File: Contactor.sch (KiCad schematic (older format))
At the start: 20 parts, among them J9 ContactorConn, Q1 NTR4003NT1G, Q2 VND5N07-E, U8 SI8261ABC-IS, U9 BAS70-04

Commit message: Moves BAS70-04 to utsvt-chips because other systems use this component
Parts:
- U9: symbol utsvt-bps:BAS70-04 -> utsvt-chips:BAS70-04
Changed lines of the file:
@@
 $EndComp
 $Comp
-L utsvt-bps:BAS70-04 U9
+L utsvt-chips:BAS70-04 U9
 U 1 1 5F133A4C
 P 8200 3500

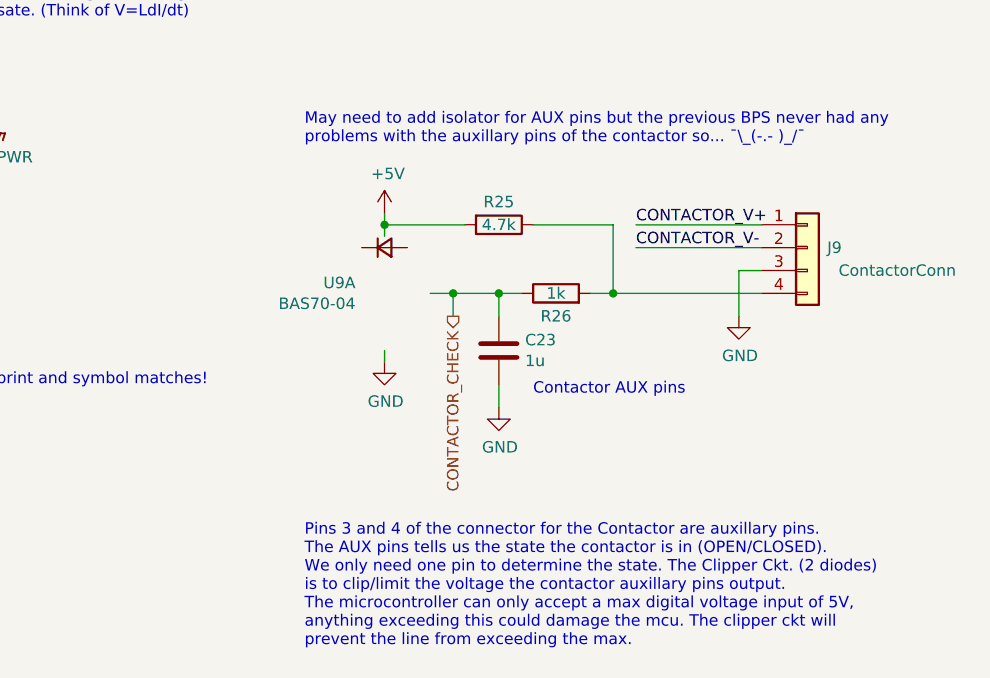
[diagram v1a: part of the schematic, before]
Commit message: Updates BAS70-04 footprint for Contactor auxillary interface
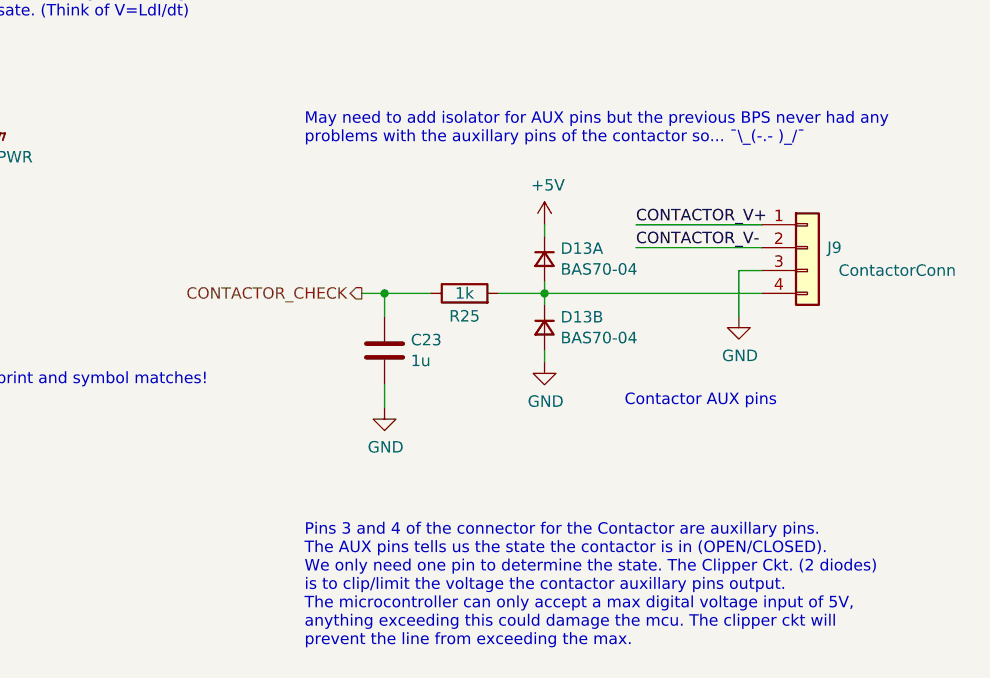
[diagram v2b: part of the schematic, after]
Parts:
- removed R25: 4.7k, Resistor_SMD:R_0805_2012Metric, symbol Device:R
- removed U9: BAS70-04, Package_TO_SOT_SMD:SOT-23, symbol utsvt-chips:BAS70-04
- added D13: BAS70-04, Package_TO_SOT_SMD:SOT-23, symbol utsvt-chips:BAS70-04
- renumbered R26 to R25
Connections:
- wire segments 78 -> 74
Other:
- moved on the sheet: C23, R25
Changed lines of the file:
@@
 $EndComp
 $Comp
-L power:GND #PWR061
+L power:GND #PWR063
 U 1 1 5C30292A
 P 9750 3800
-F 0 "#PWR061" H 9750 3550 50  0001 C CNN
+F 0 "#PWR063" H 9750 3550 50  0001 C CNN
 F 1 "GND" H 9755 3627 50  0000 C CNN
 F 2 "" H 9750 3800 50  0001 C CNN
@@
 $EndComp
 $Comp
-L Device:R R26
+L Device:R R25
 U 1 1 5C302C24
-P 8950 3700
-F 0 "R26" V 8850 3700 50  0000 C CNN
-F 1 "1k" V 8950 3700 50  0000 C CNN
-F 2 "Resistor_SMD:R_0805_2012Metric" V 8880 3700 50  0001 C CNN
-F 3 "~" H 8950 3700 50  0001 C CNN
-	1    8950 3700
+P 8550 3700
+F 0 "R25" V 8450 3700 50  0000 C CNN
+F 1 "1k" V 8550 3700 50  0000 C CNN
+F 2 "Resistor_SMD:R_0805_2012Metric" V 8480 3700 50  0001 C CNN
+F 3 "~" H 8550 3700 50  0001 C CNN
+	1    8550 3700
 	0    -1   -1   0
 $EndComp
 Wire Wire Line
 	9750 3800 9750 3600
-Wire Wire Line
-	9850 3700 9200 3700
 $Comp
 L Device:C C23
 U 1 1 5C3030F2
-P 8700 3950
-F 0 "C23" H 8815 3996 50  0000 L CNN
-F 1 "1u" H 8815 3905 50  0000 L CNN
-F 2 "Capacitor_SMD:C_0805_2012Metric" H 8738 3800 50  0001 C CNN
-F 3 "~" H 8700 3950 50  0001 C CNN
-	1    8700 3950
-	1    0    0    -1
-$EndComp
-Wire Wire Line
-	8700 3800 8700 3700
-Wire Wire Line
-	8700 3700 8800 3700
-Wire Wire Line
-	8700 4200 8700 4100
+P 8200 3950
+F 0 "C23" H 8315 3996 50  0000 L CNN
+F 1 "1u" H 8315 3905 50  0000 L CNN
+F 2 "Capacitor_SMD:C_0805_2012Metric" H 8238 3800 50  0001 C CNN
+F 3 "~" H 8200 3950 50  0001 C CNN
+	1    8200 3950
+	1    0    0    -1
+$EndComp
+Wire Wire Line
+	8200 3800 8200 3700
+Wire Wire Line
+	8200 3700 8400 3700
+Wire Wire Line
+	8200 4200 8200 4100
 $Comp
 L power:GND #PWR060
 U 1 1 5C304D16
-P 8700 4200
-F 0 "#PWR060" H 8700 3950 50  0001 C CNN
-F 1 "GND" H 8705 4027 50  0000 C CNN
-F 2 "" H 8700 4200 50  0001 C CNN
-F 3 "" H 8700 4200 50  0001 C CNN
-	1    8700 4200
-	1    0    0    -1
-$EndComp
-Connection ~ 8700 3700
-$Comp
-L power:GND #PWR059
+P 8200 4200
+F 0 "#PWR060" H 8200 3950 50  0001 C CNN
+F 1 "GND" H 8205 4027 50  0000 C CNN
+F 2 "" H 8200 4200 50  0001 C CNN
+F 3 "" H 8200 4200 50  0001 C CNN
+	1    8200 4200
+	1    0    0    -1
+$EndComp
+Connection ~ 8200 3700
+$Comp
+L power:GND #PWR062
 U 1 1 5C305432
-P 8200 4000
-F 0 "#PWR059" H 8200 3750 50  0001 C CNN
-F 1 "GND" H 8205 3827 50  0000 C CNN
-F 2 "" H 8200 4000 50  0001 C CNN
-F 3 "" H 8200 4000 50  0001 C CNN
-	1    8200 4000
-	1    0    0    -1
-$EndComp
-Wire Wire Line
-	8200 4000 8200 3950
-$Comp
-L power:+5V #PWR058
+P 8900 4000
+F 0 "#PWR062" H 8900 3750 50  0001 C CNN
+F 1 "GND" H 8905 3827 50  0000 C CNN
+F 2 "" H 8900 4000 50  0001 C CNN
+F 3 "" H 8900 4000 50  0001 C CNN
+	1    8900 4000
+	1    0    0    -1
+$EndComp
+Wire Wire Line
+	8900 4000 8900 3950
+$Comp
+L power:+5V #PWR061
 U 1 1 5C305723
-P 8200 3350
-F 0 "#PWR058" H 8200 3200 50  0001 C CNN
-F 1 "+5V" H 8215 3523 50  0000 C CNN
-F 2 "" H 8200 3350 50  0001 C CNN
-F 3 "" H 8200 3350 50  0001 C CNN
-	1    8200 3350
-	1    0    0    -1
-$EndComp
-Text HLabel 8500 3800 3    50   Output ~ 0
+P 8900 3400
+F 0 "#PWR061" H 8900 3250 50  0001 C CNN
+F 1 "+5V" H 8915 3573 50  0000 C CNN
+F 2 "" H 8900 3400 50  0001 C CNN
+F 3 "" H 8900 3400 50  0001 C CNN
+	1    8900 3400
+	1    0    0    -1
+$EndComp
+Text HLabel 8100 3700 0    50   Output ~ 0
 CONTACTOR_CHECK
-Wire Wire Line
-	8500 3800 8500 3700
-Connection ~ 8500 3700
-Wire Wire Line
-	8500 3700 8700 3700
-Wire Wire Line
-	8400 3700 8500 3700
 Wire Wire Line
 	9850 3500 9300 3500
@@
 Wire Wire Line
 	2350 3550 2350 3500
-$Comp
-L Device:R R25
-U 1 1 5C3945DD
-P 8700 3400
-F 0 "R25" V 8600 3400 50  0000 C CNN
-F 1 "4.7k" V 8700 3400 50  0000 C CNN
-F 2 "Resistor_SMD:R_0805_2012Metric" V 8630 3400 50  0001 C CNN
-F 3 "~" H 8700 3400 50  0001 C CNN
-	1    8700 3400
-	0    1    1    0
-$EndComp
-Wire Wire Line
-	8200 3350 8200 3400
-Wire Wire Line
-	8200 3400 8550 3400
-Connection ~ 8200 3400
-Wire Wire Line
-	8200 3400 8200 3450
-Wire Wire Line
-	8850 3400 9200 3400
-Wire Wire Line
-	9200 3400 9200 3700
-Connection ~ 9200 3700
-Wire Wire Line
-	9200 3700 9100 3700
-$Comp
-L power:GNDPWR #PWR056
+Wire Wire Line
+	8900 3400 8900 3450
+$Comp
+L power:GNDPWR #PWR058
 U 1 1 5C3F7F9B
 P 5800 4450
-F 0 "#PWR056" H 5800 4250 50  0001 C CNN
+F 0 "#PWR058" H 5800 4250 50  0001 C CNN
 F 1 "GNDPWR" H 5804 4296 50  0000 C CNN
 F 2 "" H 5800 4400 50  0001 C CNN
@@
 $EndComp
 $Comp
-L power:GNDPWR #PWR052
+L power:GNDPWR #PWR054
 U 1 1 5C3FD54A
 P 4400 4050
-F 0 "#PWR052" H 4400 3850 50  0001 C CNN
+F 0 "#PWR054" H 4400 3850 50  0001 C CNN
 F 1 "GNDPWR" H 4404 3896 50  0000 C CNN
 F 2 "" H 4400 4000 50  0001 C CNN
@@
 P 2350 4700
 AR Path="/5C392C6A/5C9B866F" Ref="#PWR?"  Part="1"
-AR Path="/5C38C674/5C9B866F" Ref="#PWR050"  Part="1"
-F 0 "#PWR050" H 2350 4450 50  0001 C CNN
+AR Path="/5C38C674/5C9B866F" Ref="#PWR052"  Part="1"
+F 0 "#PWR052" H 2350 4450 50  0001 C CNN
 F 1 "GND" H 2355 4527 50  0000 C CNN
 F 2 "" H 2350 4700 50  0001 C CNN
@@
 	2350 3950 2350 4000
 $Comp
-L power:+5V #PWR051
+L power:+5V #PWR053
 U 1 1 5C3C25EA
 P 2800 3000
-F 0 "#PWR051" H 2800 2850 50  0001 C CNN
+F 0 "#PWR053" H 2800 2850 50  0001 C CNN
 F 1 "+5V" H 2815 3173 50  0000 C CNN
 F 2 "" H 2800 3000 50  0001 C CNN
@@
 	4400 3750 4400 3850
 $Comp
-L power:+12V #PWR055
+L power:+12V #PWR057
 U 1 1 5C30CB9C
 P 5800 2800
-F 0 "#PWR055" H 5800 2650 50  0001 C CNN
+F 0 "#PWR057" H 5800 2650 50  0001 C CNN
 F 1 "+12V" H 5815 2973 50  0000 C CNN
 F 2 "" H 5800 2800 50  0001 C CNN
@@
 	6500 2950 6500 2900
 $Comp
-L power:GNDPWR #PWR057
+L power:GNDPWR #PWR059
 U 1 1 5C3F88F8
 P 6500 2950
-F 0 "#PWR057" H 6500 2750 50  0001 C CNN
+F 0 "#PWR059" H 6500 2750 50  0001 C CNN
 F 1 "GNDPWR" H 6504 2796 50  0000 C CNN
 F 2 "" H 6500 2900 50  0001 C CNN
@@
 Text Notes 7850 5250 0    50   ~ 0
 Pins 3 and 4 of the connector for the Contactor are auxillary pins.\nThe AUX pins tells us the state the contactor is in (OPEN/CLOSED).\nWe only need one pin to determine the state. The Clipper Ckt. (2 diodes)\nis to clip/limit the voltage the contactor auxillary pins output.\nThe microcontroller can only accept a max digital voltage input of 5V,\nanything exceeding this could damage the mcu. The clipper ckt will\nprevent the line from exceeding the max.
-Text Notes 8850 4150 0    50   ~ 0
+Text Notes 9250 4200 0    50   ~ 0
 Contactor AUX pins
 Text Notes 5900 2500 0    50   ~ 0
@@
 $EndComp
 $Comp
-L utsvt-chips:BAS70-04 U9
-U 1 1 5F133A4C
-P 8200 3500
-F 0 "U9" H 8073 3346 50  0000 R CNN
-F 1 "BAS70-04" H 8073 3255 50  0000 R CNN
-F 2 "Package_TO_SOT_SMD:SOT-23" H 8650 3500 50  0001 C CNN
-F 3 "" H 8650 3500 50  0001 C CNN
-	1    8200 3500
-	1    0    0    -1
-$EndComp
-$Comp
-L power:GNDPWR #PWR054
+L power:GNDPWR #PWR056
 U 1 1 5C3F8405
 P 5200 2750
-F 0 "#PWR054" H 5200 2550 50  0001 C CNN
+F 0 "#PWR056" H 5200 2550 50  0001 C CNN
 F 1 "GNDPWR" H 5204 2596 50  0000 C CNN
 F 2 "" H 5200 2700 50  0001 C CNN
@@
 $EndComp
 $Comp
-L power:+12V #PWR053
+L power:+12V #PWR055
 U 1 1 5C30FC6C
 P 5200 2250
-F 0 "#PWR053" H 5200 2100 50  0001 C CNN
+F 0 "#PWR055" H 5200 2100 50  0001 C CNN
 F 1 "+12V" H 5215 2423 50  0000 C CNN
 F 2 "" H 5200 2250 50  0001 C CNN
@@
 Text Notes 2650 4750 0    50   ~ 0
 Local (Leader Board) GND\n(Internal)
+Wire Wire Line
+	8100 3700 8200 3700
+$Comp
+L utsvt-chips:BAS70-04 D13
+U 1 1 5F36D1F4
+P 8900 3550
+F 0 "D13" V 8854 3620 50  0000 L CNN
+F 1 "BAS70-04" V 8945 3620 50  0000 L CNN
+F 2 "Package_TO_SOT_SMD:SOT-23" V 8900 3550 50  0001 C CNN
+F 3 "~" V 8900 3550 50  0001 C CNN
+	1    8900 3550
+	0    1    1    0
+$EndComp
+$Comp
+L utsvt-chips:BAS70-04 D13
+U 2 1 5F36DC30
+P 8900 3850
+F 0 "D13" V 8854 3920 50  0000 L CNN
+F 1 "BAS70-04" V 8945 3920 50  0000 L CNN
+F 2 "Package_TO_SOT_SMD:SOT-23" V 8900 3850 50  0001 C CNN
+F 3 "~" V 8900 3850 50  0001 C CNN
+	2    8900 3850
+	0    1    1    0
+$EndComp
+Wire Wire Line
+	8900 3750 8900 3700
+Wire Wire Line
+	8900 3700 9850 3700
+Connection ~ 8900 3700
+Wire Wire Line
+	8900 3700 8900 3650
+Wire Wire Line
+	8700 3700 8900 3700
 $EndSCHEMATC
